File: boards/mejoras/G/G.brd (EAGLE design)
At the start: 100 x 45 mm, 34 parts, among them J1 XT60-M, J2 XT60-M, J3 XT60-M, J4 XT60-M, J5 XT60-M, J6 XT60-M, Q1 IRFR7440PBF, Q2 IRFR7440PBF

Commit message: changes to g circuit
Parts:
- L1: value MSS7341 -> DR125; device inductor-coilcraft:MSS7341 -> inductors:DR125
- moved LED1 12.2 mm to (69.0, 26.6), turned to 0 degrees
- moved R15 11.9 mm to (57.8, 6.37), flipped to the bottom, turned to 180 degrees
- moved C5 8.97 mm to (36.9, 30.6)
- moved R2 8.78 mm to (76.1, 16.6)
- moved Q1 7.41 mm to (48.0, 35.7), turned to 90 degrees
- moved R6 6.14 mm to (74.2, 26.2)
- moved L1 3.36 mm to (62.8, 16.3)
- moved R5 2.22 mm to (63.2, 15.8)
- moved C4 1.17 mm to (46.8, 18.0), turned to 90 degrees
- moved C2 0.79 mm to (29.2, 16.4), turned to 135 degrees
- moved R4 0.50 mm to (64.4, 8.09)
- moved D2 0.45 mm to (35.1, 12.7)
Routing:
- net PWM2: track 17.4 -> 3.86 mm, vias 1 -> 0
- net N$13: track 35.7 -> 49.2 mm
- net N$1: track 25.9 -> 13.0 mm
- net N$16: track 59.2 -> 47.9 mm
- net N$14: track 26.3 -> 36.4 mm, vias 1 -> 2
- net IN1A: track 3.65 -> 13.0 mm
- net N$15: track 31.6 -> 39.9 mm
- net N$12: track 33.9 -> 42.0 mm
- net N$9: track 39.6 -> 46.9 mm
- net VPOWER: track 165.7 -> 168.8 mm
- net N$4: track 2.10 -> 4.09 mm
- net N$11: track 29.8 -> 28.2 mm
- net N$10: track 23.9 -> 25.4 mm
- net 5V: track 154.8 -> 153.3 mm
- net N$5: track 19.8 -> 18.8 mm
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
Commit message: corrected bug
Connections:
- removed net POWER: U$2.12
- net VPOWER: now also U$2.12
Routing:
- net VPOWER: track 168.8 -> 191.0 mm
- net N$18: track 83.8 -> 79.0 mm, vias 1 -> 3
- net N$2: track 10.5 -> 9.23 mm
- net N$5: track 18.8 -> 19.6 mm
- net N$9: track 46.9 -> 47.4 mm

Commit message: udpated new circuits
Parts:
- added R1, R16: (no value), rcl:M1206
- moved R7 1.70 mm to (60.3, 41.7)
- moved LED1 1.03 mm to (69.5, 25.7)
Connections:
- new net N$19: R1.1, U$1.8
- new net N$20: R16.1, U$2.8
- net GND: now also R1.2, R16.2
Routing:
- net N$20: track 0.00 -> 31.9 mm, vias 0 -> 1
- net N$19: track 0.00 -> 30.9 mm, vias 0 -> 1
- net GND: track 311.5 -> 321.6 mm, vias 9 -> 10
- net N$18: track 79.0 -> 72.3 mm
- net OUT4: track 75.0 -> 68.7 mm
- net N$17: track 48.1 -> 46.0 mm
- net 5V: track 153.4 -> 151.3 mm
- net OUT3: track 82.0 -> 80.6 mm
- net N$2: track 9.23 -> 10.5 mm
- net N$9: track 47.4 -> 48.6 mm
- net N$12: track 42.0 -> 40.9 mm
- net N$15: track 39.9 -> 38.8 mm
- net N$11: track 28.2 -> 27.3 mm
- net N$4: track 4.09 -> 3.22 mm

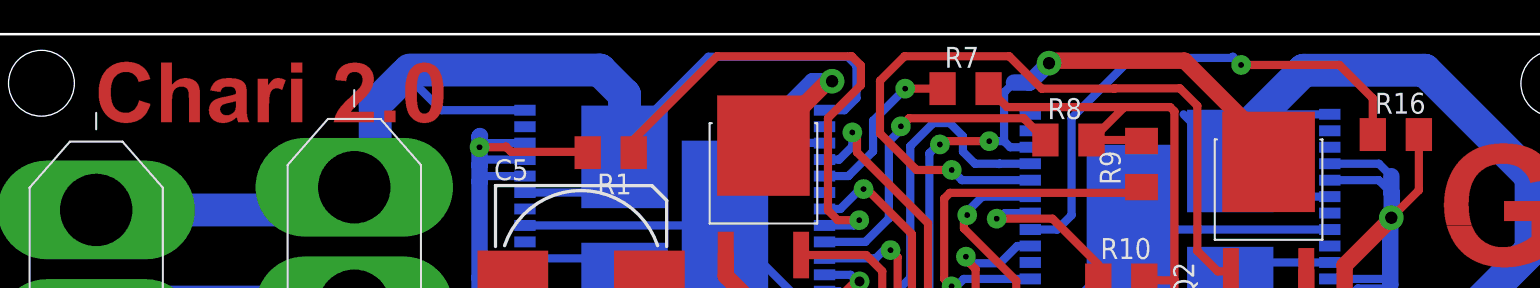
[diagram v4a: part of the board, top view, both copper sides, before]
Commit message: small fixes to g and i
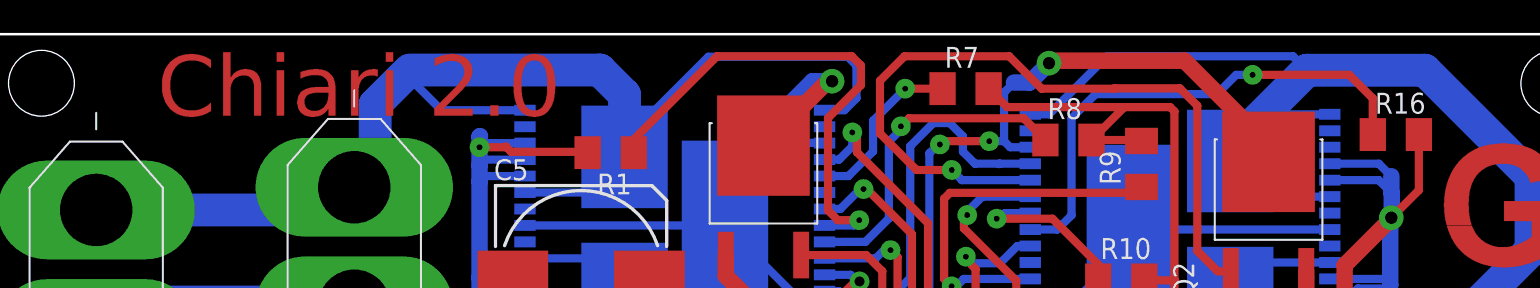
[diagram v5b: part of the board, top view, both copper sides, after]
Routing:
- net OUT4: track 68.7 -> 83.2 mm
- net N$20: track 31.9 -> 31.0 mm
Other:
- board text added: "C:/Users/Ariel/GitHub/Sumo-Robot-Programs-Database/boards/mejoras/I/chiari.bmp"
